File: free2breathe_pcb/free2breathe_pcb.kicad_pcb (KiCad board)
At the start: 2 copper layers, 108.5 x 115 mm, 101 parts, among them J1 USB4110-GF-A_REVB, J2 LED_Connector, J3 Alarm_Connector, Q1 AO3401A, Q2 DMN3404L, SW1 Power_Switch, U1 IP5328, U2 MCP6044-E/P, U3 MCP6044-E/P, U4 SO2 Sensor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

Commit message: more routing
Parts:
- H1, H2, H3, H4, H5: footprint MountingHole:MountingHole_3.2mm_M3 -> MountingHole:MountingHole_3.2mm_M3_Pad_Via
- moved C17 11.4 mm to (107.8, 86.0)
- moved R4 9.84 mm to (104.9, 117.2)
- moved R8 9.55 mm to (135.1, 117.1), turned to 0 degrees
- moved D4 8.15 mm to (135.0, 112.5), turned to -90 degrees
- moved C16 7.59 mm to (105.6, 86.0)
- moved R6 6.93 mm to (124.9, 117.1), turned to 0 degrees
- moved R5 6.92 mm to (115.0, 117.1)
- moved D1 6.91 mm to (105.0, 112.5), turned to -90 degrees
- moved C15 5.80 mm to (103.4, 86.0)
- moved L1 4.67 mm to (101.0, 79.2), turned to -90 degrees
- moved D3 4.08 mm to (125.0, 112.5), turned to -90 degrees
- moved D2 3.29 mm to (115.0, 112.5), turned to -90 degrees
- moved R12 2.91 mm to (105.3, 148.0)
- moved C18 2.80 mm to (103.7, 145.2)
- moved H5 2.55 mm to (160.0, 115.0)
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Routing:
- net /Arduino_3V3: track 0.00 -> 157.2 mm, vias 0 -> 6
- net /Arduino_A1: track 0.00 -> 125.3 mm, vias 0 -> 2
- net /Arduino_A0: track 0.00 -> 104.9 mm
- net /VBAT+: track 0.00 -> 103.0 mm
- net /Arduino_A3: track 2.73 -> 76.0 mm, vias 0 -> 2
- net /Arduino_A2: track 2.73 -> 73.1 mm
- net /VOUT: track 0.00 -> 69.5 mm, vias 0 -> 1
- net GND: track 68.5 -> 0.00 mm
- net /Arduino_D13: track 0.00 -> 64.1 mm
- net /Divider_High: track 3.59 -> 62.2 mm
- net /Arduino_D12: track 0.00 -> 48.9 mm
- net /Arduino_D9: track 0.00 -> 48.9 mm
- net /Arduino_D10: track 0.00 -> 44.9 mm
- net /Arduino_A6: track 0.00 -> 43.3 mm, vias 0 -> 2
- net /Arduino_D11: track 0.00 -> 39.8 mm
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
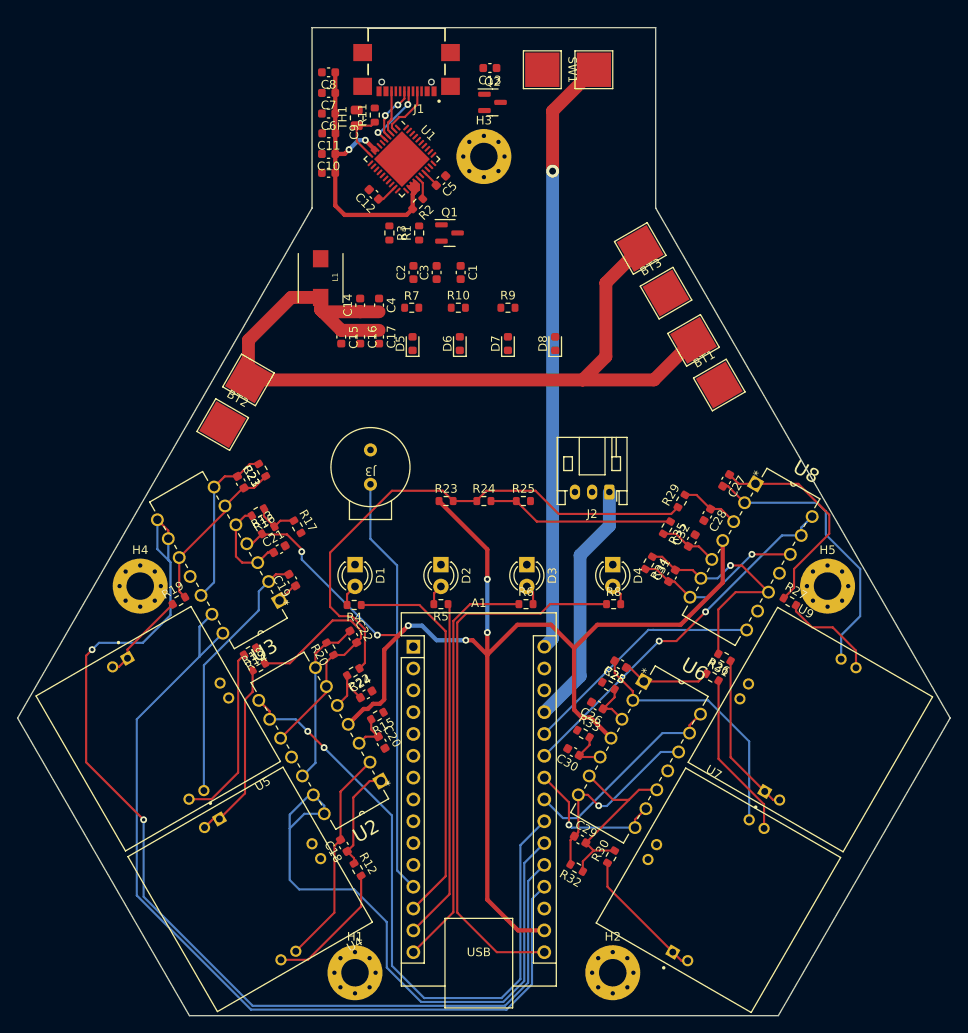
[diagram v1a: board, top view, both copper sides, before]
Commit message: add 3d models
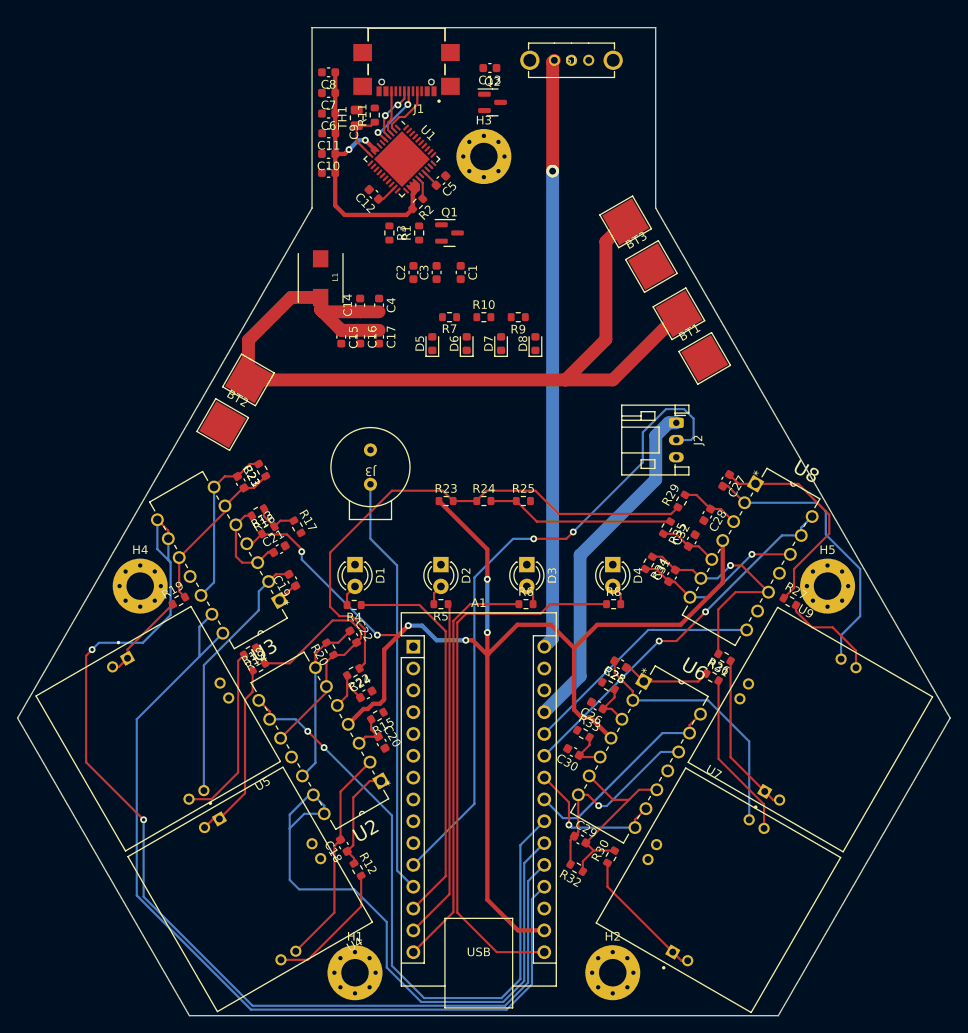
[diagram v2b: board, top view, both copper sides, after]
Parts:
- removed SW1: Power_Switch, switch:switch_pad
- added S1: EG1213, components:SW_EG1213, F.Cu at (130.2, 53.8)
- moved J2 11.2 mm to (142.4, 96.0), turned to -90 degrees
- moved R7 4.54 mm to (116.0, 83.7), turned to 180 degrees
- moved BT1 3.53 mm to (144.2, 85.9)
- moved BT3 3.53 mm to (138.0, 75.2)
- moved R10 3.17 mm to (120.0, 83.7)
- moved D8 2.30 mm to (126.0, 86.8)
- moved D5 2.30 mm to (114.0, 86.8)
- moved R9 1.63 mm to (124.0, 83.7), turned to 180 degrees
- moved D6 0.80 mm to (118.0, 86.8)
- moved D7 0.80 mm to (122.0, 86.8)
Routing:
- net /Arduino_D8: track 0.00 -> 76.8 mm, vias 0 -> 2
- net /Arduino_5V: track 28.8 -> 40.6 mm
- net /VBAT+: track 103.0 -> 105.8 mm
- net /VOUT: track 69.5 -> 68.7 mm

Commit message: update step file to include standard components
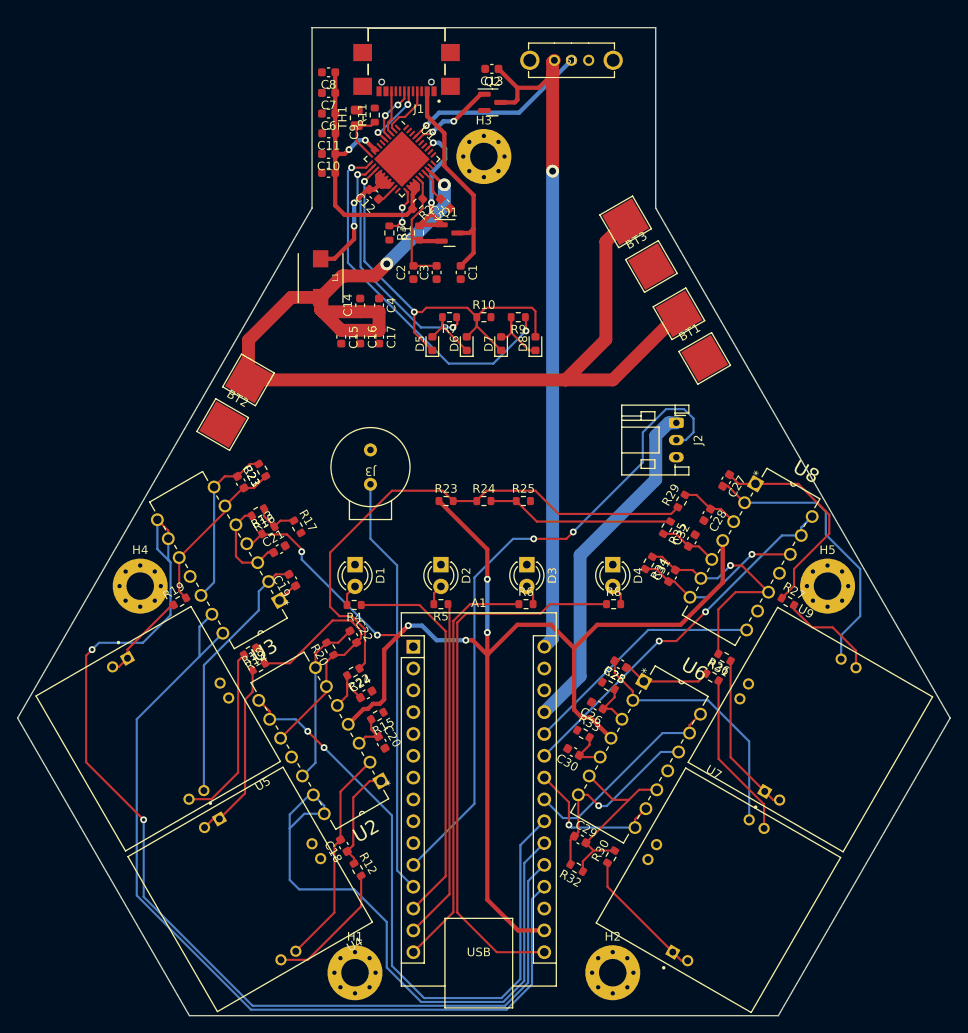
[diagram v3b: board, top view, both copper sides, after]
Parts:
- moved C5 2.75 mm to (115.5, 70.5), turned to 135 degrees
- moved C13 0.25 mm to (120.9, 54.8)
- moved R27 0.23 mm to (155.4, 116.8)
- moved R19 0.14 mm to (84.6, 116.8)
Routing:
- net Net-(D5-Pad1): track 0.00 -> 51.1 mm, vias 0 -> 2
- net Net-(R9-Pad1): track 0.00 -> 42.5 mm, vias 0 -> 2
- net /VBAT+: track 105.8 -> 134.5 mm, vias 0 -> 2
- net Net-(R7-Pad1): track 0.00 -> 28.3 mm, vias 0 -> 2
- net /VBUS: track 0.00 -> 25.2 mm
- net Net-(U1-Pad37): track 0.00 -> 21.9 mm, vias 0 -> 1
- net Net-(C12-Pad2): track 0.00 -> 19.4 mm, vias 0 -> 2
- net /VBUSG: track 0.00 -> 18.6 mm, vias 0 -> 2
- net /VMID: track 2.58 -> 17.4 mm
- net /VOUT: track 68.7 -> 80.1 mm
- net /VOUTG: track 0.00 -> 9.90 mm, vias 0 -> 2
- net Net-(D7-Pad2): track 0.00 -> 8.66 mm
- net Net-(D5-Pad2): track 0.00 -> 7.08 mm
- net Net-(R3-Pad1): track 0.00 -> 5.70 mm, vias 0 -> 2
- net /VREG: track 2.07 -> 3.91 mm

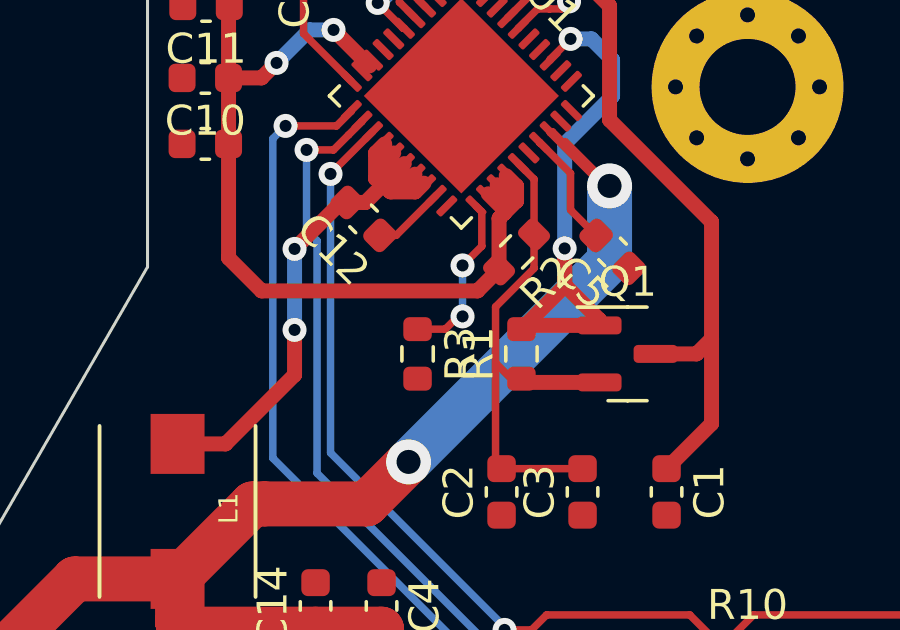
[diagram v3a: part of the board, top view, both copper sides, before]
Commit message: update components and todo, swap current-sense resistor to 0805
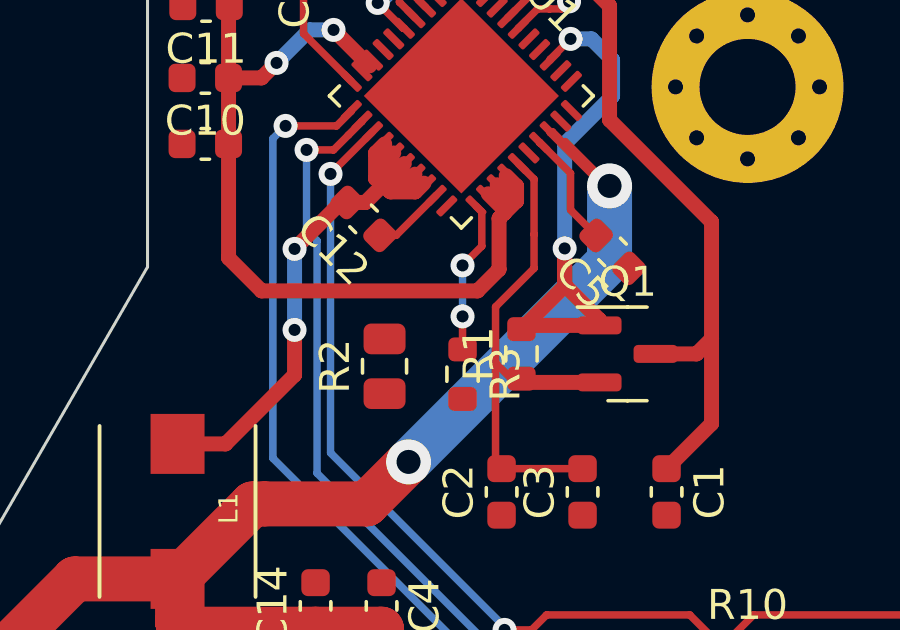
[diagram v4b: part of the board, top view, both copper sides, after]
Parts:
- R2: footprint Resistor_SMD:R_0603_1608Metric -> Resistor_SMD:R_0805_2012Metric
- moved R2 5.82 mm to (107.9, 74.3), turned to 90 degrees
- moved R3 1.64 mm to (110.5, 74.6)
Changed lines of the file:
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@@
   (net 91 "Net-(R31-Pad1)")
   (net 92 "unconnected-(U1-Pad20)")
-  (net 93 "Net-(U1-Pad37)")
+  (net 93 "Net-(S1-Pad2)")
   (net 94 "unconnected-(U1-Pad1)")
   (net 95 "unconnected-(U1-Pad6)")
@@
       (net 113 "unconnected-(S1-Pad1)") (pintype "passive+no_connect"))
     (pad "2" thru_hole circle locked (at 0 0 180) (size 1.308 1.308) (drill 0.8) (layers *.Cu *.Mask)
-      (net 93 "Net-(U1-Pad37)") (pintype "passive"))
+      (net 93 "Net-(S1-Pad2)") (pintype "passive"))
     (pad "3" thru_hole circle locked (at 2 0 180) (size 1.308 1.308) (drill 0.8) (layers *.Cu *.Mask)
       (net 29 "/VOUT") (pintype "passive"))
@@
   )
   (footprint "Resistor_SMD:R_0603_1608Metric" (layer "F.Cu")
-    (at 109 73.9 -90)
+    (at 110.5 74.575 -90)
     (descr "Resistor SMD 0603 (1608 Metric), square (rectangular) end terminal, IPC_7351 nominal, (Body size source: IPC-SM-782 page 72, https://www.pcb-3d.com/wordpress/wp-content/uploads/ipc-sm-782a_amendment_1_and_2.pdf), generated with kicad-footprint-generator")
     (tags "resistor")
@@
       (net 75 "/VOUTG") (pinfunction "VOUT1G") (pintype "input"))
     (pad "37" smd roundrect locked (at -0.75 -2.9375 315) (size 0.25 0.825) (layers "F.Cu" "F.Paste" "F.Mask") (roundrect_rratio 0.25)
-      (net 93 "Net-(U1-Pad37)") (pinfunction "VOUT1") (pintype "input"))
+      (net 93 "Net-(S1-Pad2)") (pinfunction "VOUT1") (pintype "input"))
     (pad "38" smd roundrect locked (at -1.25 -2.9375 315) (size 0.25 0.825) (layers "F.Cu" "F.Paste" "F.Mask") (roundrect_rratio 0.25)
       (net 102 "unconnected-(U1-Pad38)") (pinfunction "DMA1") (pintype "input+no_connect"))
@@
     )
   )
-  (footprint "Resistor_SMD:R_0603_1608Metric" (layer "F.Cu")
-    (at 112.3 70.5 -135)
-    (descr "Resistor SMD 0603 (1608 Metric), square (rectangular) end terminal, IPC_7351 nominal, (Body size source: IPC-SM-782 page 72, https://www.pcb-3d.com/wordpress/wp-content/uploads/ipc-sm-782a_amendment_1_and_2.pdf), generated with kicad-footprint-generator")
+  (footprint "Resistor_SMD:R_0805_2012Metric" (layer "F.Cu")
+    (at 107.9 74.3125 90)
+    (descr "Resistor SMD 0805 (2012 Metric), square (rectangular) end terminal, IPC_7351 nominal, (Body size source: IPC-SM-782 page 72, https://www.pcb-3d.com/wordpress/wp-content/uploads/ipc-sm-782a_amendment_1_and_2.pdf), generated with kicad-footprint-generator")
     (tags "resistor")
     (property "Sheetfile" "free2breathe_pcb.kicad_sch")
     (property "Sheetname" "")
     (attr smd)
-    (fp_text reference "R2" (at 0 -1.43 45) (layer "F.SilkS")
+    (fp_text reference "R2" (at 0 -1.65 90) (layer "F.SilkS")
       (effects (font (size 1 1) (thickness 0.15)))
     )
-    (fp_text value "10m" (at 0 1.43 45) (layer "F.Fab")
+    (fp_text value "10m" (at 0 1.65 90) (layer "F.Fab")
       (effects (font (size 1 1) (thickness 0.15)))
     )
-    (fp_text user "${REFERENCE}" (at 0 0 45) (layer "F.Fab")
-      (effects (font (size 0.4 0.4) (thickness 0.06)))
+    (fp_text user "${REFERENCE}" (at 0 0 90) (layer "F.Fab")
+      (effects (font (size 0.5 0.5) (thickness 0.08)))
     )
-    (fp_line (start -0.237258 -0.5225) (end 0.237258 -0.5225) (layer "F.SilkS") (width 0.12))
-    (fp_line (start -0.237258 0.5225) (end 0.237258 0.5225) (layer "F.SilkS") (width 0.12))
-    (fp_line (start -1.48 -0.73) (end 1.48 -0.73) (layer "F.CrtYd") (width 0.05))
-    (fp_line (start 1.48 0.73) (end -1.48 0.73) (layer "F.CrtYd") (width 0.05))
-    (fp_line (start 1.48 -0.73) (end 1.48 0.73) (layer "F.CrtYd") (width 0.05))
-    (fp_line (start -1.48 0.73) (end -1.48 -0.73) (layer "F.CrtYd") (width 0.05))
-    (fp_line (start -0.8 -0.4125) (end 0.8 -0.4125) (layer "F.Fab") (width 0.1))
-    (fp_line (start 0.8 -0.4125) (end 0.8 0.4125) (layer "F.Fab") (width 0.1))
-    (fp_line (start 0.8 0.4125) (end -0.8 0.4125) (layer "F.Fab") (width 0.1))
-    (fp_line (start -0.8 0.4125) (end -0.8 -0.4125) (layer "F.Fab") (width 0.1))
-    (pad "1" smd roundrect (at -0.825 0 225) (size 0.8 0.95) (layers "F.Cu" "F.Paste" "F.Mask") (roundrect_rratio 0.25)
+    (fp_line (start -0.227064 -0.735) (end 0.227064 -0.735) (layer "F.SilkS") (width 0.12))
+    (fp_line (start -0.227064 0.735) (end 0.227064 0.735) (layer "F.SilkS") (width 0.12))
+    (fp_line (start 1.68 -0.95) (end 1.68 0.95) (layer "F.CrtYd") (width 0.05))
+    (fp_line (start -1.68 -0.95) (end 1.68 -0.95) (layer "F.CrtYd") (width 0.05))
+    (fp_line (start -1.68 0.95) (end -1.68 -0.95) (layer "F.CrtYd") (width 0.05))
+    (fp_line (start 1.68 0.95) (end -1.68 0.95) (layer "F.CrtYd") (width 0.05))
+    (fp_line (start -1 0.625) (end -1 -0.625) (layer "F.Fab") (width 0.1))
+    (fp_line (start 1 0.625) (end -1 0.625) (layer "F.Fab") (width 0.1))
+    (fp_line (start 1 -0.625) (end 1 0.625) (layer "F.Fab") (width 0.1))
+    (fp_line (start -1 -0.625) (end 1 -0.625) (layer "F.Fab") (width 0.1))
+    (pad "1" smd roundrect (at -0.9125 0 90) (size 1.025 1.4) (layers "F.Cu" "F.Paste" "F.Mask") (roundrect_rratio 0.243902)
       (net 33 "/VMID") (pintype "passive"))
-    (pad "2" smd roundrect (at 0.825 0 225) (size 0.8 0.95) (layers "F.Cu" "F.Paste" "F.Mask") (roundrect_rratio 0.25)
+    (pad "2" smd roundrect (at 0.9125 0 90) (size 1.025 1.4) (layers "F.Cu" "F.Paste" "F.Mask") (roundrect_rratio 0.243902)
       (net 34 "/VSYS") (pintype "passive"))
-    (model "${KICAD6_3DMODEL_DIR}/Resistor_SMD.3dshapes/R_0603_1608Metric.wrl"
+    (model "${KICAD6_3DMODEL_DIR}/Resistor_SMD.3dshapes/R_0805_2012Metric.wrl"
       (offset (xyz 0 0 0))
       (scale (xyz 1 1 1))
@@
   (segment (start 111.141637 69.163135) (end 110.946618 68.968116) (width 0.25) (layer "F.Cu") (net 78))
   (segment (start 111.141637 70.308863) (end 111.141637 69.163135) (width 0.25) (layer "F.Cu") (net 78))
-  (segment (start 110.3505 72.6495) (end 109.925 73.075) (width 0.25) (layer "F.Cu") (net 78))
-  (segment (start 109.925 73.075) (end 109 73.075) (width 0.25) (layer "F.Cu") (net 78))
+  (segment (start 110.5 72.6495) (end 110.5 73.75) (width 0.25) (layer "F.Cu") (net 78))
   (segment (start 110.5 70.9505) (end 111.141637 70.308863) (width 0.25) (layer "F.Cu") (net 78))
   (segment (start 110.5 72.6495) (end 110.3505 72.6495) (width 0.25) (layer "F.Cu") (net 78))
